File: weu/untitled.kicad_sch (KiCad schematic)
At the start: 1 part

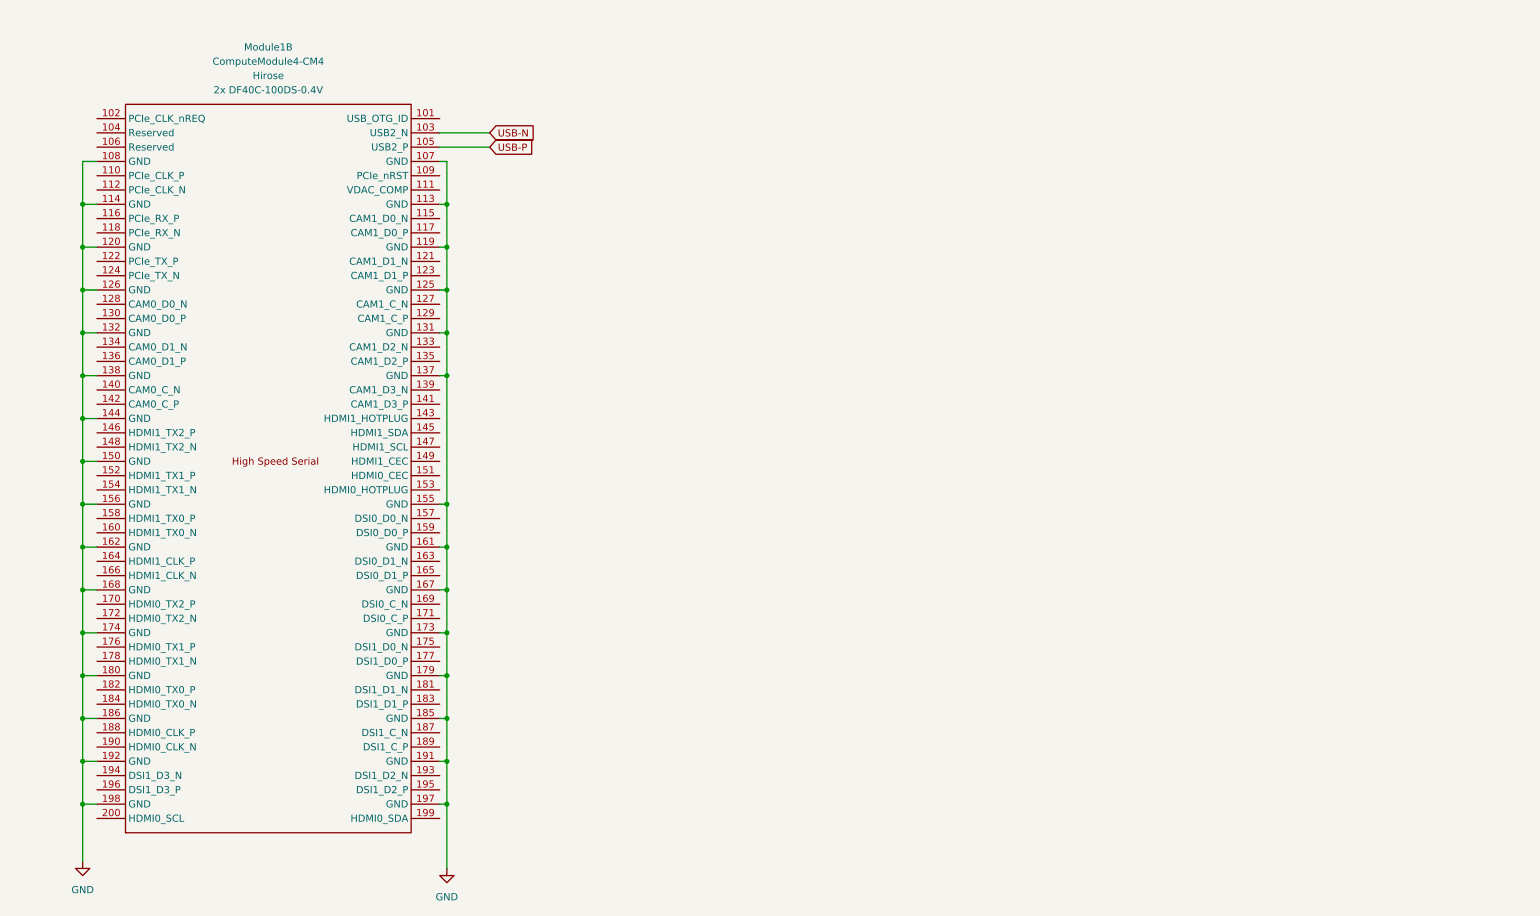
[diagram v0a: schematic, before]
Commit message: Added hdmi
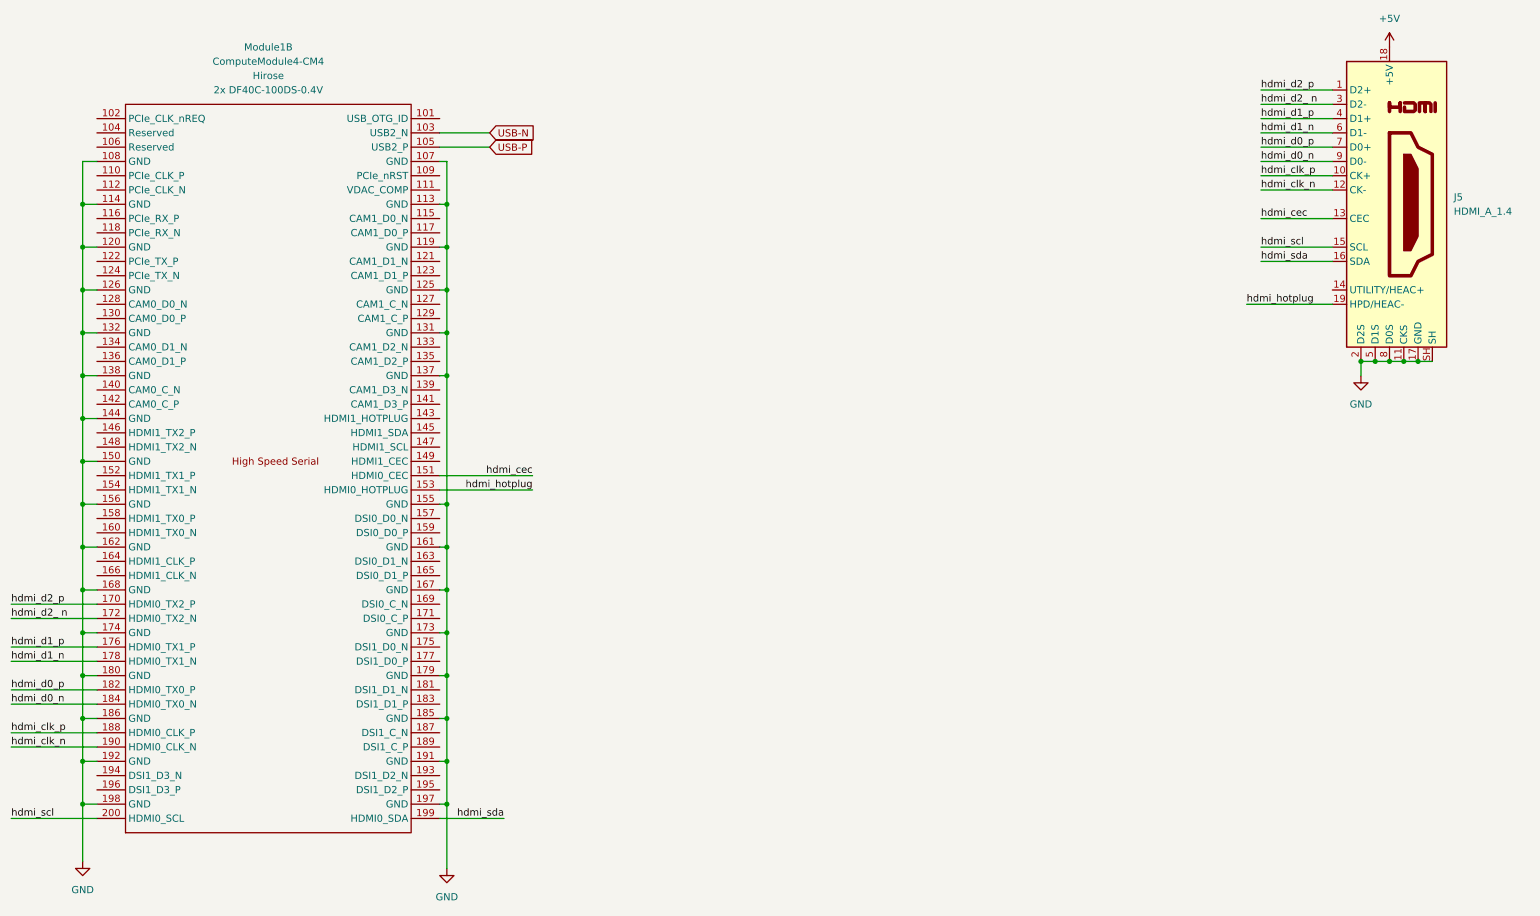
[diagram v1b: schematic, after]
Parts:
- added J5: HDMI_A_1.4, symbol Connector:HDMI_A_1.4
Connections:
- net GND: now also J5.11 (CKS), J5.17 (GND), J5.2 (D2S), J5.5 (D1S), J5.8 (D0S), J5.SH
- net hdmi_cec: now reaches Module1.151 (HDMI0_CEC)
- net hdmi_cec: now also J5.13 (CEC)
- net hdmi_hotplug: now reaches Module1.153 (HDMI0_HOTPLUG)
- net hdmi_hotplug: now also J5.19 (HPD/HEAC-)
- net hdmi_d2_p: now reaches Module1.170 (HDMI0_TX2_P)
- net hdmi_d2_p: now also J5.1 (D2+)
- net hdmi_d2_ n: now reaches Module1.172 (HDMI0_TX2_N)
- net hdmi_d2_ n: now also J5.3 (D2-)
- net hdmi_d1_p: now reaches Module1.176 (HDMI0_TX1_P)
- net hdmi_d1_p: now also J5.4 (D1+)
- net hdmi_d1_n: now reaches Module1.178 (HDMI0_TX1_N)
- net hdmi_d1_n: now also J5.6 (D1-)
- net hdmi_d0_p: now reaches Module1.182 (HDMI0_TX0_P)
- net hdmi_d0_p: now also J5.7 (D0+)
- net hdmi_d0_n: now reaches Module1.184 (HDMI0_TX0_N)
- net hdmi_d0_n: now also J5.9 (D0-)
- net hdmi_clk_p: now reaches Module1.188 (HDMI0_CLK_P)
- net hdmi_clk_p: now also J5.10 (CK+)
- net hdmi_clk_n: now reaches Module1.190 (HDMI0_CLK_N)
- net hdmi_clk_n: now also J5.12 (CK-)
- net hdmi_sda: now reaches Module1.199 (HDMI0_SDA)
- net hdmi_sda: now also J5.16 (SDA)
- net hdmi_scl: now reaches Module1.200 (HDMI0_SCL)
- net hdmi_scl: now also J5.15 (SCL)
- new net +5V: J5.18 (+5V)
